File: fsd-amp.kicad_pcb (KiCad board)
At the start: 2 copper layers, 100 x 60 mm, 17 parts, among them J1001 Screw_Terminal_01x06, J1004 AudioJack2_Ground_Switch, Q1001 FZT 653 ZET, Q1002 FZT 653 ZET, Q1003 FZT 753 ZET

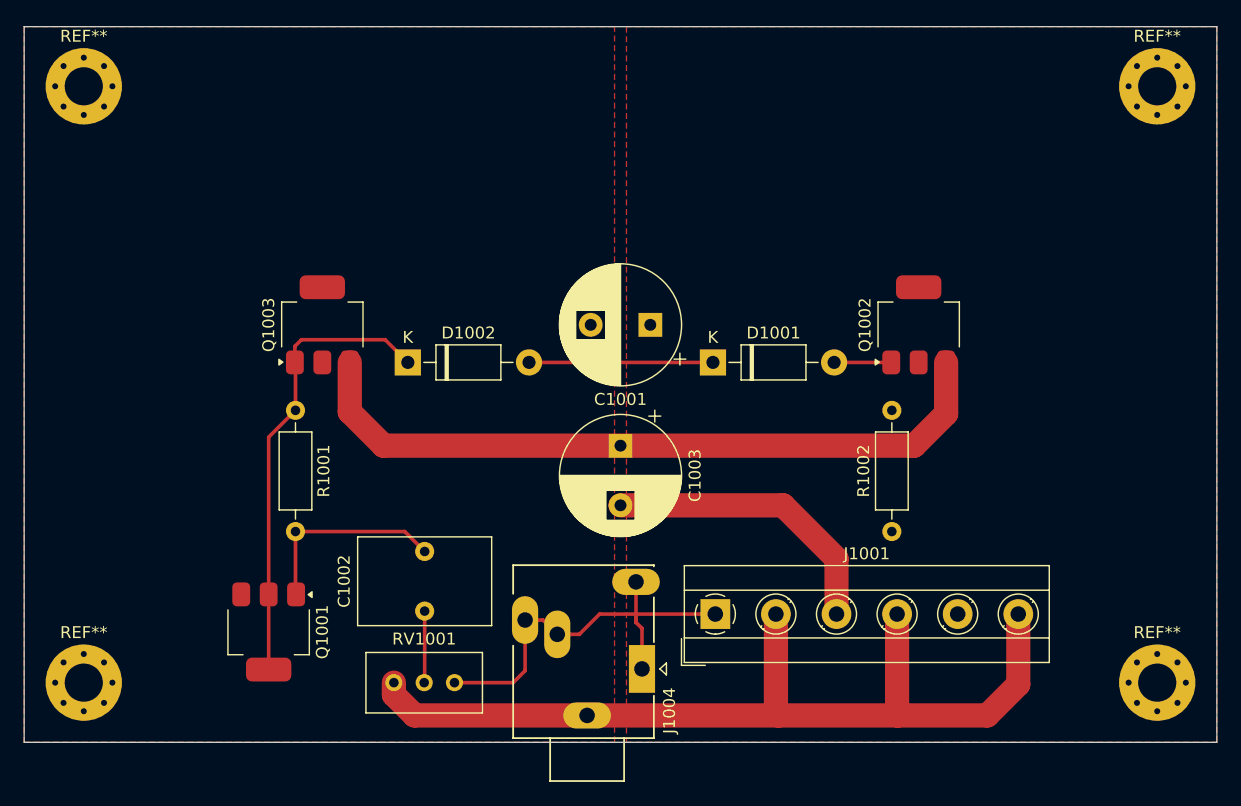
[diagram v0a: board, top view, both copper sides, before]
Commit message: add fill zone bottom side
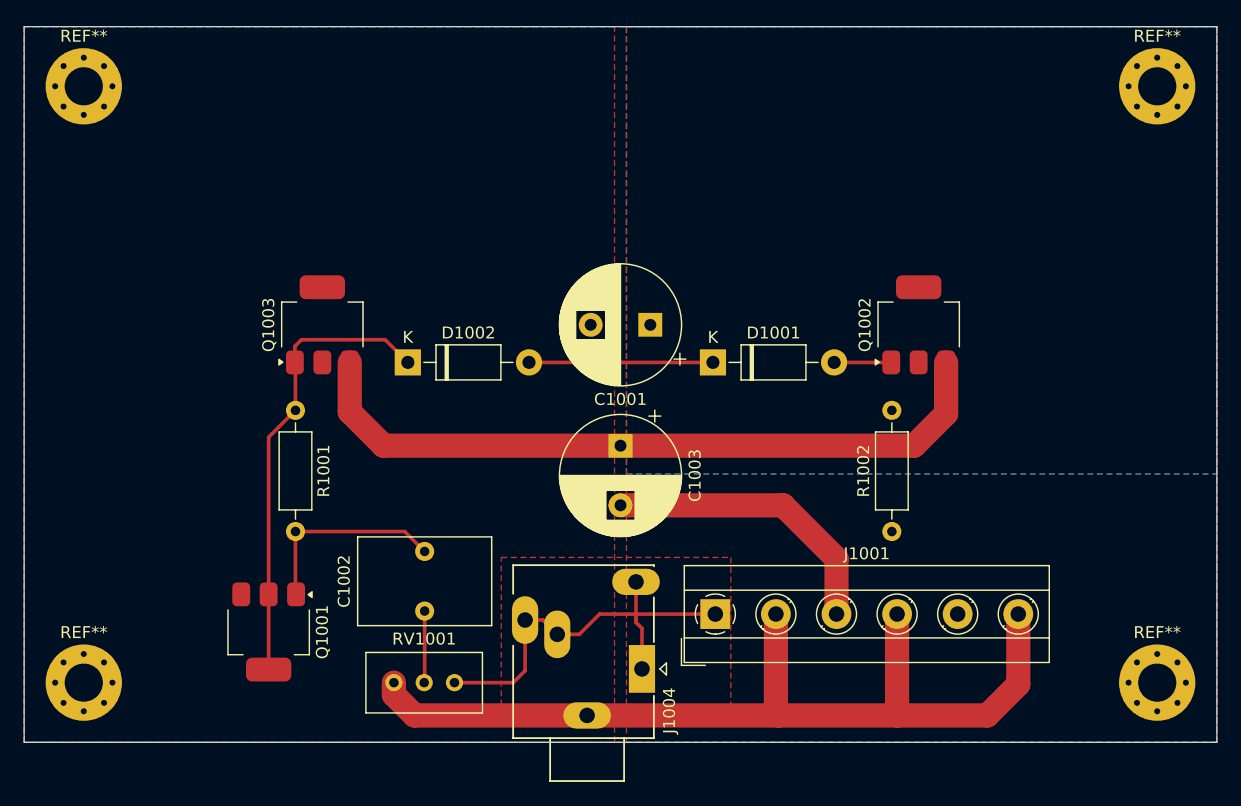
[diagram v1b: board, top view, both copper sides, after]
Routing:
- added copper zone on B.Cu, net +9V
- added copper zone on F.Cu, net /amp_in
- added copper zone on B.Cu, net GND
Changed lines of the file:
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@@
+	)
+	(zone
+		(net 10)
+		(net_name "/amp_in")
+		(layer "F.Cu")
+		(hatch edge 0.5)
+		(priority 3)
+		(connect_pads thru_hole_only
+			(clearance 0.5)
+		)
+		(min_thickness 0.25)
+		(filled_areas_thickness no)
+		(fill yes
+			(thermal_gap 0.5)
+			(thermal_bridge_width 1)
+		)
+		(polygon
+			(pts
+				(xy 159.25 94.5) (xy 159.25 107.75) (xy 140 107.75) (xy 140 94.5)
+			)
+		)
 	)
 	(zone
@@
 			)
 		)
+	)
+	(zone
+		(net 2)
+		(net_name "GND")
+		(layer "B.Cu")
+		(hatch edge 0.5)
+		(priority 1)
+		(connect_pads thru_hole_only
+			(clearance 0.5)
+		)
+		(min_thickness 0.25)
+		(filled_areas_thickness no)
+		(fill yes
+			(thermal_gap 0.5)
+			(thermal_bridge_width 1)
+		)
+		(polygon
+			(pts
+				(xy 100 50) (xy 200 50) (xy 200 110) (xy 100 110)
+			)
+		)
+	)
+	(zone
+		(net 1)
+		(net_name "+9V")
+		(layer "B.Cu")
+		(hatch edge 0.5)
+		(priority 3)
+		(connect_pads thru_hole_only
+			(clearance 0.5)
+		)
+		(min_thickness 0.25)
+		(filled_areas_thickness no)
+		(fill yes
+			(thermal_gap 0.5)
+			(thermal_bridge_width 1)
+		)
+		(polygon
+			(pts
+				(xy 150.5 50) (xy 150.5 87.5) (xy 200 87.5) (xy 200 50)
+			)
+		)

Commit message: add thermal relief for transistors
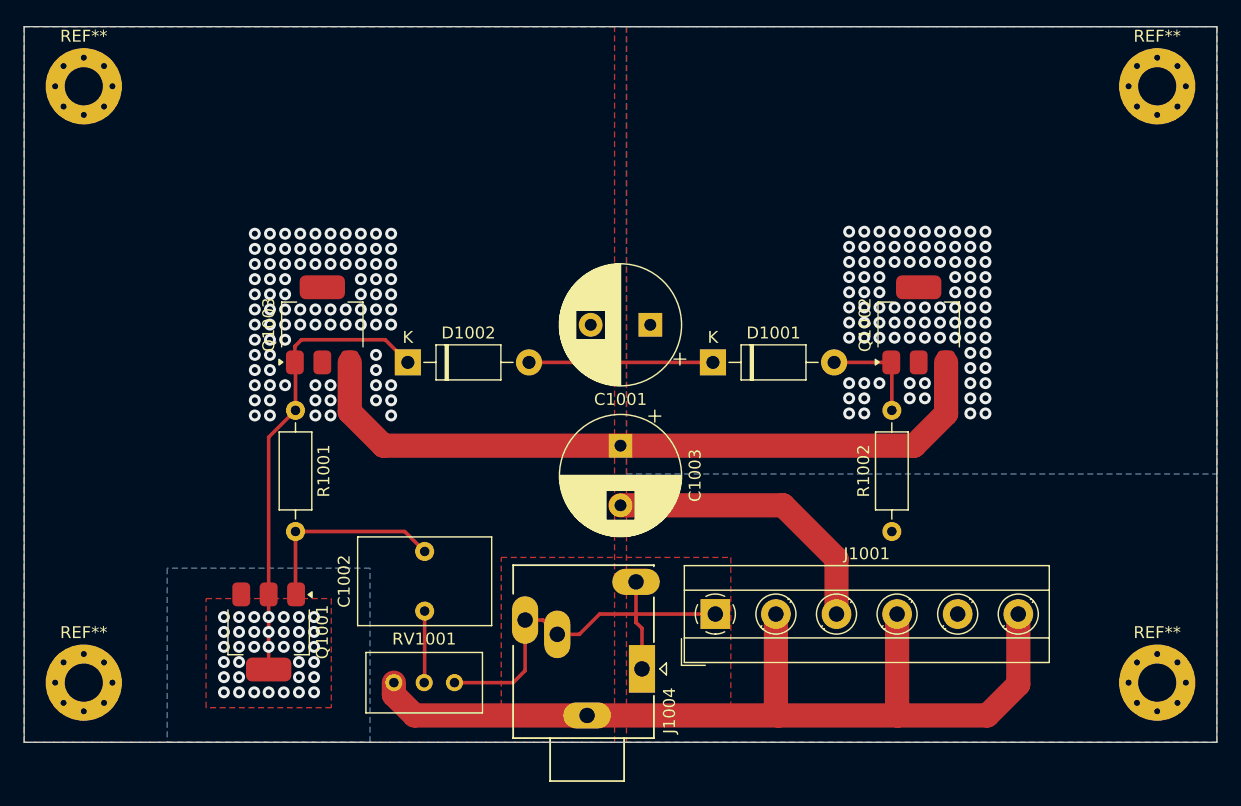
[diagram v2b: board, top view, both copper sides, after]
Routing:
- net Net-(D1001-A): track 4.79 -> 8.83 mm
- net Net-(D1002-K): vias 0 -> 36
- net GND: vias 0 -> 89
- net +9V: vias 0 -> 93
- added copper zone on B.Cu, net Net-(D1002-K)
- added copper zone on F.Cu, net Net-(D1002-K)

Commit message: fix drc errors
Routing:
- net GND: vias 89 -> 83
- net +9V: vias 93 -> 90

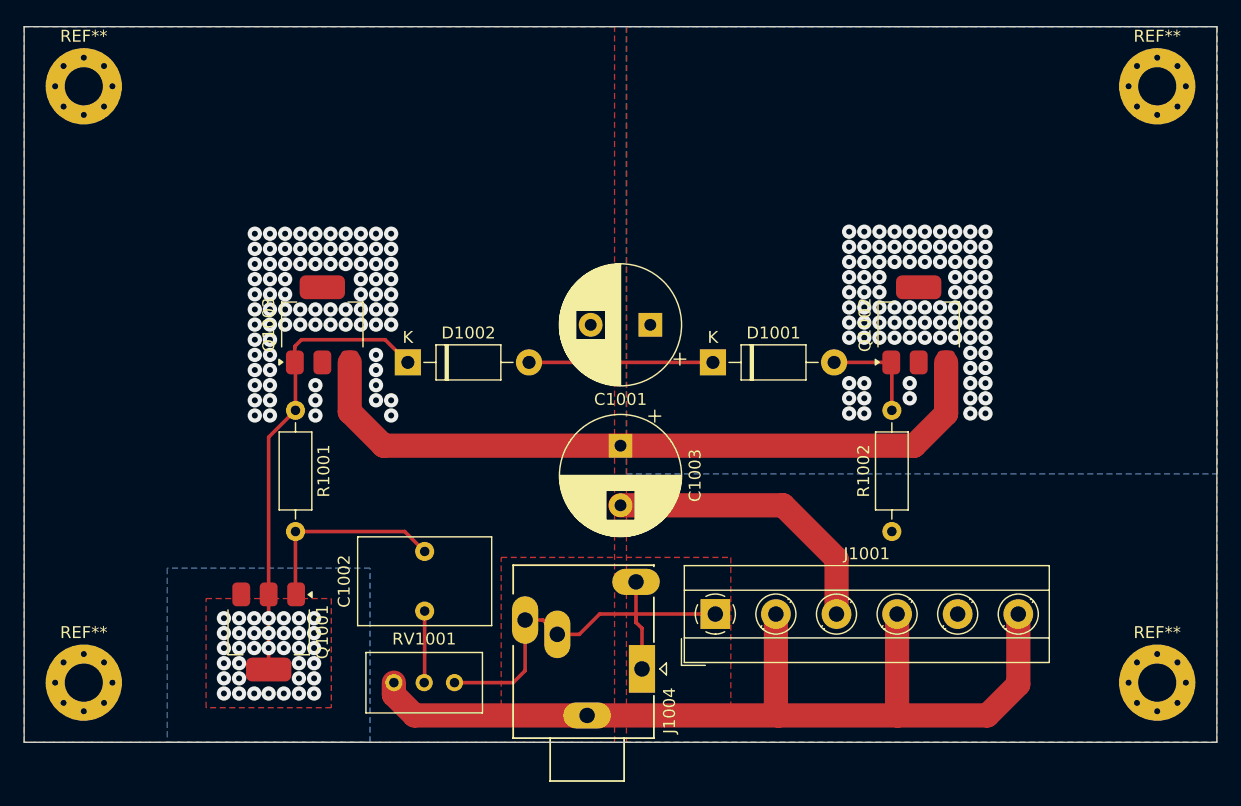
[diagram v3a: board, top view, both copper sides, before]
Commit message: fix drc warnings, enhace silkscreen
- fix drc warnings (silk screen related)
- move mounting holes to 'fp' library
- enhance silkscreen placement
- remove outline silkscreen from SOT-223 footprint
- remove silkscreen out of board from audion jack
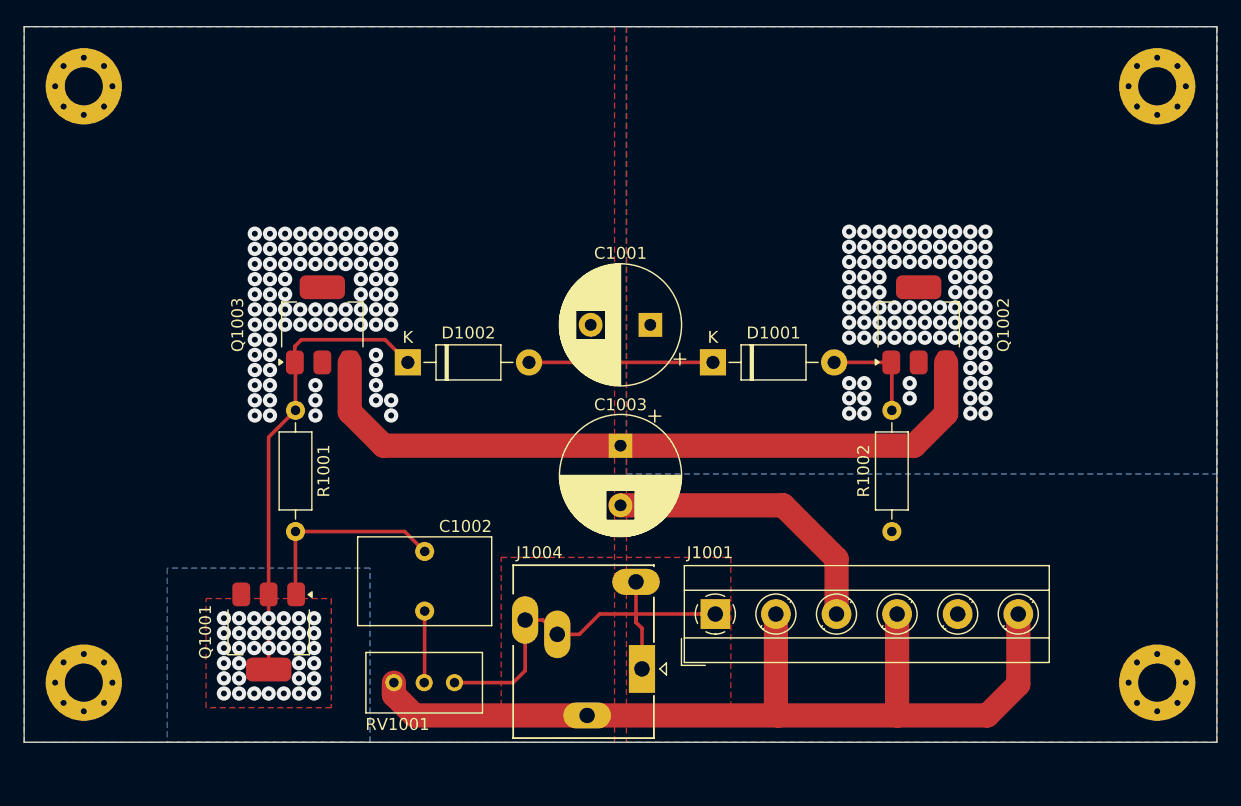
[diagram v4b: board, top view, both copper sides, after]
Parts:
- REF** (x4): footprint MountingHole:MountingHole_3.2mm_M3_Pad_Via -> fp:MountingHole_3.2mm_M3_Pad_Via
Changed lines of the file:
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@@
 		(tags "CP Radial series Radial pin pitch 5.00mm  diameter 10mm Electrolytic Capacitor")
 		(property "Reference" "C1003"
-			(at 2.5 -6.25 90)
+			(at -3.432323 0 180)
 			(layer "F.SilkS")
 			(effects
@@
 		(tags "Potentiometer vertical Bourns 3296W")
 		(property "Reference" "RV1001"
-			(at -2.54 -3.66 360)
+			(at -4.78 3.5 180)
 			(layer "F.SilkS")
 			(effects
@@
 		(tags "C Rect series Radial pin pitch 5.00mm  length 7.2mm width 11mm Capacitor")
 		(property "Reference" "C1002"
-			(at 2.5 -6.75 270)
+			(at 7.1 3.42 0)
 			(layer "F.SilkS")
 			(effects
@@
 		(tags "CP Radial series Radial pin pitch 5.00mm  diameter 10mm Electrolytic Capacitor")
 		(property "Reference" "C1001"
-			(at 2.5 -6.25 180)
+			(at 2.5 6 180)
 			(layer "F.SilkS")
 			(effects
@@
 		)
 	)
-	(footprint "MountingHole:MountingHole_3.2mm_M3_Pad_Via"
+	(footprint "fp:MountingHole_3.2mm_M3_Pad_Via"
 		(layer "F.Cu")
 		(at 105 55)
@@
 			(at 0 -4.2 0)
 			(layer "F.SilkS")
+			(hide yes)
 			(effects
 				(font
@@
 			)
 		)
-		(property "Footprint" "MountingHole:MountingHole_3.2mm_M3_Pad_Via"
+		(property "Footprint" "fp:MountingHole_3.2mm_M3_Pad_Via"
 			(at 0 0 0)
 			(unlocked yes)
@@
 		)
 	)
-	(footprint "MountingHole:MountingHole_3.2mm_M3_Pad_Via"
+	(footprint "fp:MountingHole_3.2mm_M3_Pad_Via"
 		(layer "F.Cu")
 		(at 195 55)
@@
 			(at 0 -4.2 0)
 			(layer "F.SilkS")
+			(hide yes)
 			(effects
 				(font
@@
 			)
 		)
-		(property "Footprint" "MountingHole:MountingHole_3.2mm_M3_Pad_Via"
+		(property "Footprint" "fp:MountingHole_3.2mm_M3_Pad_Via"
 			(at 0 0 0)
 			(unlocked yes)
@@
 		)
 	)
-	(footprint "MountingHole:MountingHole_3.2mm_M3_Pad_Via"
+	(footprint "fp:MountingHole_3.2mm_M3_Pad_Via"
 		(layer "F.Cu")
 		(at 195 105)
@@
 			(at 0 -4.2 0)
 			(layer "F.SilkS")
+			(hide yes)
 			(effects
 				(font
@@
 			)
 		)
-		(property "Footprint" "MountingHole:MountingHole_3.2mm_M3_Pad_Via"
+		(property "Footprint" "fp:MountingHole_3.2mm_M3_Pad_Via"
 			(at 0 0 0)
 			(unlocked yes)
@@
 		(tags "jack stereo TRS")
 		(property "Reference" "J1004"
-			(at -3.5 2.3 -90)
+			(at 9.75 -8.6 0)
 			(layer "F.SilkS")
 			(effects
@@
 		)
 		(fp_line
-			(start -5.8 -7.7)
-			(end -9.4 -7.7)
-			(stroke
-				(width 0.15)
-				(type solid)
-			)
-			(layer "F.SilkS")
-		)
-		(fp_line
-			(start -9.4 -7.7)
-			(end -9.4 -1.5)
-			(stroke
-				(width 0.15)
-				(type solid)
-			)
-			(layer "F.SilkS")
-		)
-		(fp_line
-			(start -9.4 -1.5)
-			(end -5.8 -1.5)
-			(stroke
-				(width 0.15)
-				(type solid)
-			)
-			(layer "F.SilkS")
-		)
-		(fp_line
 			(start 8.7 1)
 			(end 8.6 1)
@@
 		)
 		(fp_line
-			(start -9.3 -7.6)
-			(end -5.7 -7.6)
-			(stroke
-				(width 0.1)
-				(type solid)
-			)
-			(layer "F.Fab")
-		)
-		(fp_line
-			(start -9.3 -7.6)
-			(end -9.3 -1.6)
-			(stroke
-				(width 0.1)
-				(type solid)
-			)
-			(layer "F.Fab")
-		)
-		(fp_line
-			(start -9.3 -1.6)
-			(end -5.7 -1.6)
-			(stroke
-				(width 0.1)
-				(type solid)
-			)
-			(layer "F.Fab")
-		)
-		(fp_line
 			(start 8.6 0.9)
 			(end 8.6 -10.7)
@@
 		)
 	)
-	(footprint "MountingHole:MountingHole_3.2mm_M3_Pad_Via"
+	(footprint "fp:MountingHole_3.2mm_M3_Pad_Via"
 		(layer "F.Cu")
 		(at 105 105)
@@
 			(at 0 -4.2 0)
 			(layer "F.SilkS")
+			(hide yes)
 			(effects
 				(font
@@
 			)
 		)
-		(property "Footprint" "MountingHole:MountingHole_3.2mm_M3_Pad_Via"
+		(property "Footprint" "fp:MountingHole_3.2mm_M3_Pad_Via"
 			(at 0 0 0)
 			(unlocked yes)
@@
 		(tags "CMS SOT")
 		(property "Reference" "Q1001"
-			(at 0 -4.5 90)
+			(at 0 5.3 90)
 			(layer "F.SilkS")
 			(effects
@@
 		(tags "CMS SOT")
 		(property "Reference" "Q1002"
-			(at 0 -4.5 -90)
+			(at 0 7.1 -90)
 			(layer "F.SilkS")
 			(effects
@@
 		(tags "CMS SOT")
 		(property "Reference" "Q1003"
-			(at 0 -4.5 -90)
+			(at 0 -7.1 -90)
 			(layer "F.SilkS")
 			(effects
@@
 		(tags "THT terminal block Metz Connect Type101_RT01606HBWC pitch 5.08mm size 30.5x8mm^2 drill 1.3mm pad 2.5mm")
 		(property "Reference" "J1001"
-			(at 12.7 -5.06 0)
+			(at -0.45 -5.15 180)
 			(layer "F.SilkS")
 			(effects

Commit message: add backup THT transistor footprint
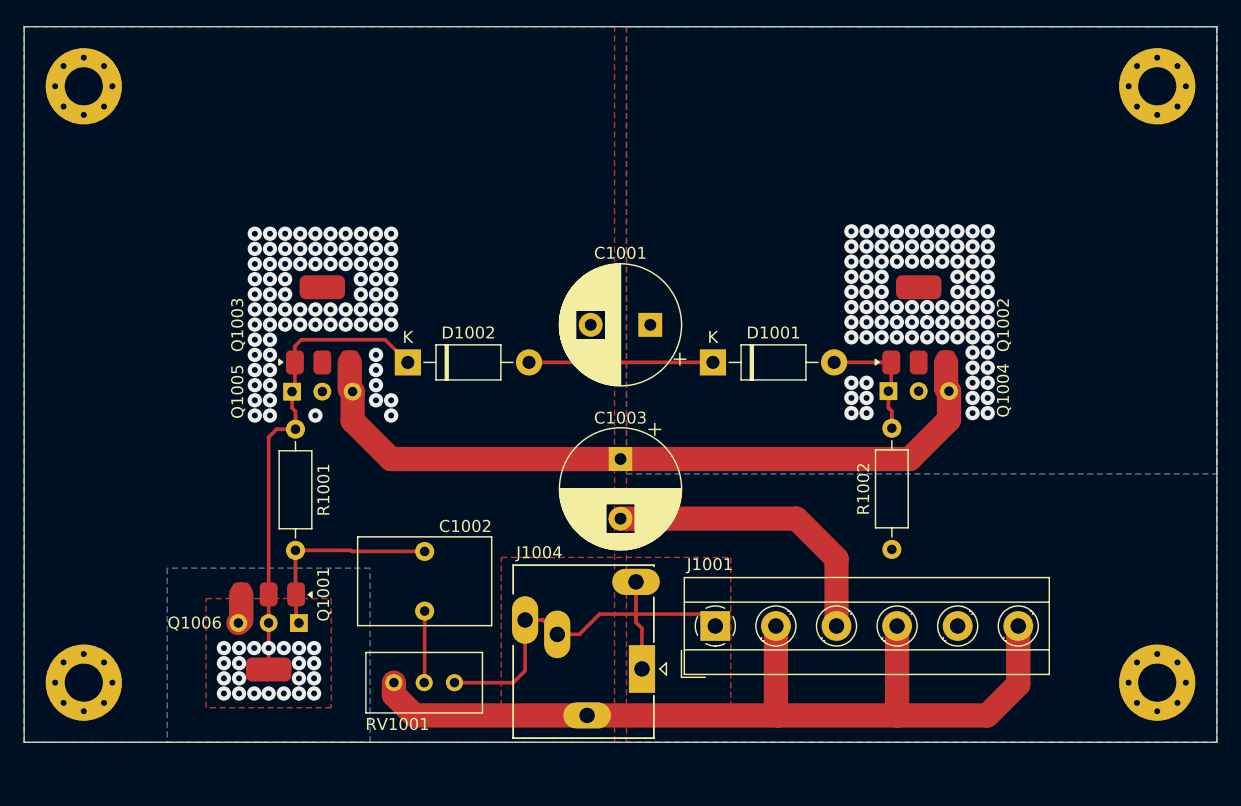
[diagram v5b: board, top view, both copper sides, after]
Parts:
- added Q1004: Q_NPN_BCE, fp:TO-92_Inline_Wide_NOcourtyard, F.Cu at (172.5, 80.6)
- added Q1005: Q_PNP_BCE, fp:TO-92_Inline_Wide_NOcourtyard, F.Cu at (122.5, 80.6)
- added Q1006: Q_NPN_BCE, fp:TO-92_Inline_Wide_NOcourtyard, F.Cu at (123.0, 100.0)
- moved R1001 1.58 mm to (122.8, 83.8)
- moved R1002 1.50 mm to (172.8, 93.8)
- moved C1003 1.12 mm to (150.0, 86.2)
- moved J1001 1.00 mm to (157.9, 100.2)
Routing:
- net Net-(Q1002-E): track 60.7 -> 62.6 mm
- net Net-(D1001-A): track 8.83 -> 10.7 mm
- net Net-(D1002-K): track 38.5 -> 39.7 mm, vias 36 -> 22
- net /amp_out: track 24.6 -> 25.1 mm
- net GND: track 78.2 -> 77.7 mm, vias 83 -> 81
- net +9V: vias 90 -> 88
